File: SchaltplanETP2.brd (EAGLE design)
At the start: 110 x 60 mm, 59 parts, among them IC1 LM2674, IC2 ZXLD1350, IC3 ZXLD1350, IC4 ZXLD1350, IC5 ZXLD1350, M1 RN42_BLUETOOTH, T1 BUK98150-55A

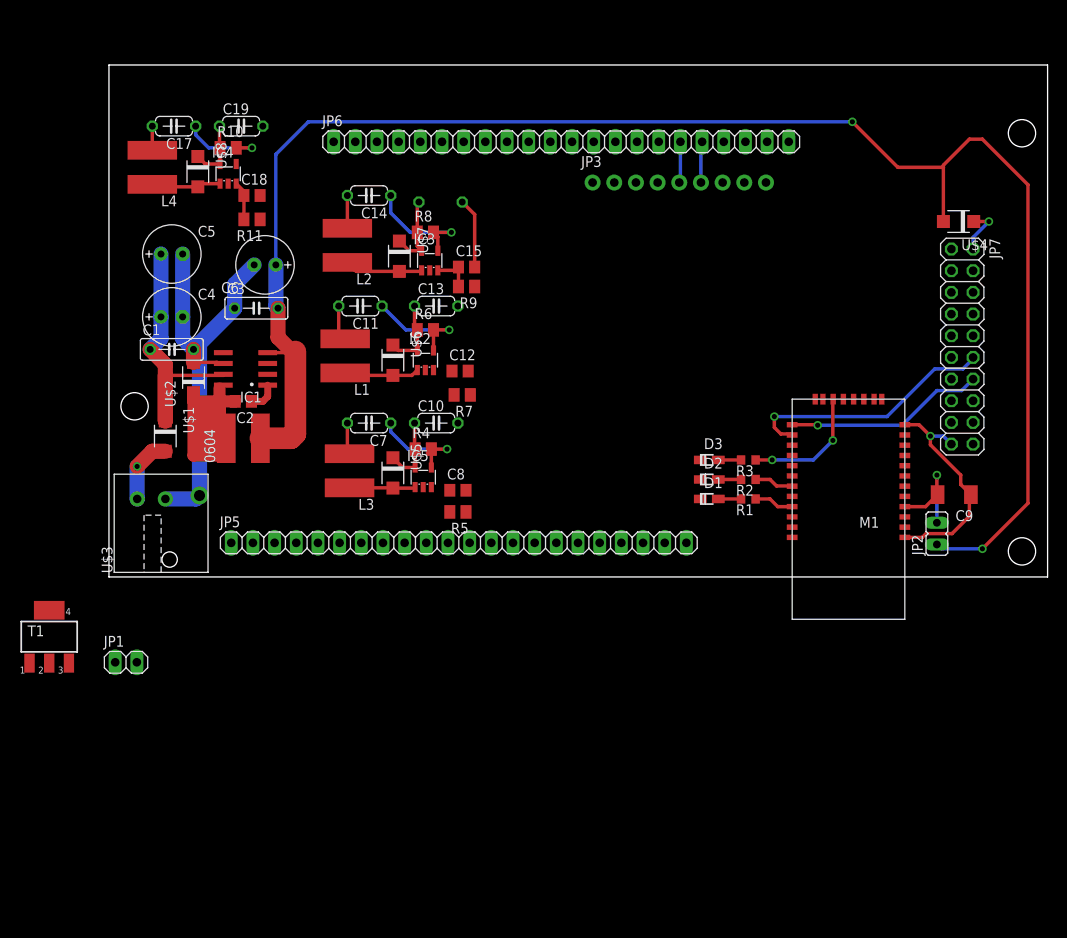
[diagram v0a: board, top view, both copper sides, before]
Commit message: Changed LED of pin 21 from the RN42 module to fit the datasheet. Added Jumpber behind DC-Jack to allow direct soldering of cables. Added Terminal Blocks for LEDs.
Placed part onto grid.
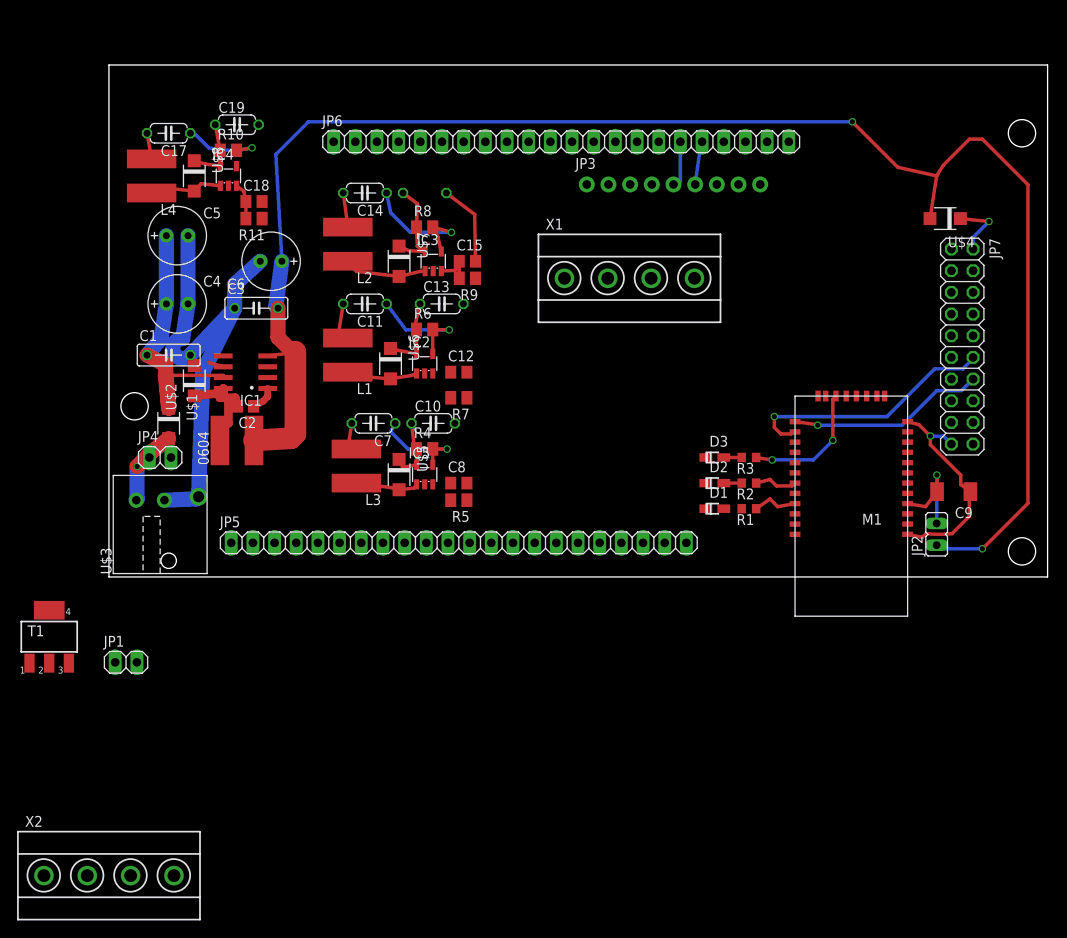
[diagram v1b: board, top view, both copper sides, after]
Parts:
- added JP4: (no value), pinhead:1X02
- added X1, X2: TERMINAL_BLOCK_MC000036, Moodlight:TERMINAL_BLOCK_MC000036
- R1: value 330 -> 220
- moved C5 2.25 mm to (8.00, 40.0)
- moved C16 2.14 mm to (37.0, 45.0)
- moved C4 1.65 mm to (8.00, 32.0)
- moved U$4 1.61 mm to (98.0, 42.0)
- moved U$1 1.54 mm to (7.00, 18.0)
- moved R5 1.38 mm to (41.0, 9.00)
- moved D1 1.31 mm to (71.0, 8.00)
- moved R1 1.15 mm to (75.0, 8.00)
- moved C17 1.04 mm to (7.00, 52.0)
- moved L4 1.01 mm to (5.00, 47.0)
- moved L3 0.98 mm to (29.0, 13.0)
- moved R9 0.97 mm to (42.0, 35.0)
- moved C8 0.85 mm to (41.0, 11.0)
- moved C6 0.83 mm to (19.0, 37.0)
- moved 0604 0.79 mm to (15.0, 16.0)
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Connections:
- removed net N$1: U$1.A, U$3.1
- new net +24V_EINGANG: JP4.1, U$1.A, U$3.1
- new net 4_LED+: X2.4
- new net 4_LED-: X2.3
- new net N$21: M1.22
- net +3V3: now also D1.A
- net 1_LED+: now also X1.2
- net 1_LED-: now also X1.1
- net 2_LED+: now also X1.4
- net 2_LED-: now also X1.3
- net 3_LED+: now also X2.2
- net 3_LED-: now also X2.1
- net GND: now also JP4.2; no longer D1.C
- net N$7: now also D1.C; no longer D1.A
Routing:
- net +24V_EINGANG: track 0.00 -> 8.93 mm, vias 0 -> 1
- net N$1: track 7.85 -> 0.00 mm, vias 1 -> 0
- net N$3: track 21.5 -> 14.1 mm
- net VCC: track 33.3 -> 36.3 mm
- net N$7: track 2.67 -> 0.00 mm
- net N$4: track 5.77 -> 7.36 mm
- net 2_LED+: track 14.6 -> 15.7 mm
- net GND: track 92.1 -> 93.1 mm
- net 0_LED-: track 3.69 -> 4.44 mm
- net N$18: track 8.21 -> 8.92 mm
- net IMP_TX: track 4.83 -> 5.53 mm
- net N$10: track 4.66 -> 5.32 mm
- net N$9: track 2.67 -> 2.10 mm
- net N$8: track 2.67 -> 2.10 mm
- net N$16: track 9.19 -> 9.71 mm

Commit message: added terminal header and connection
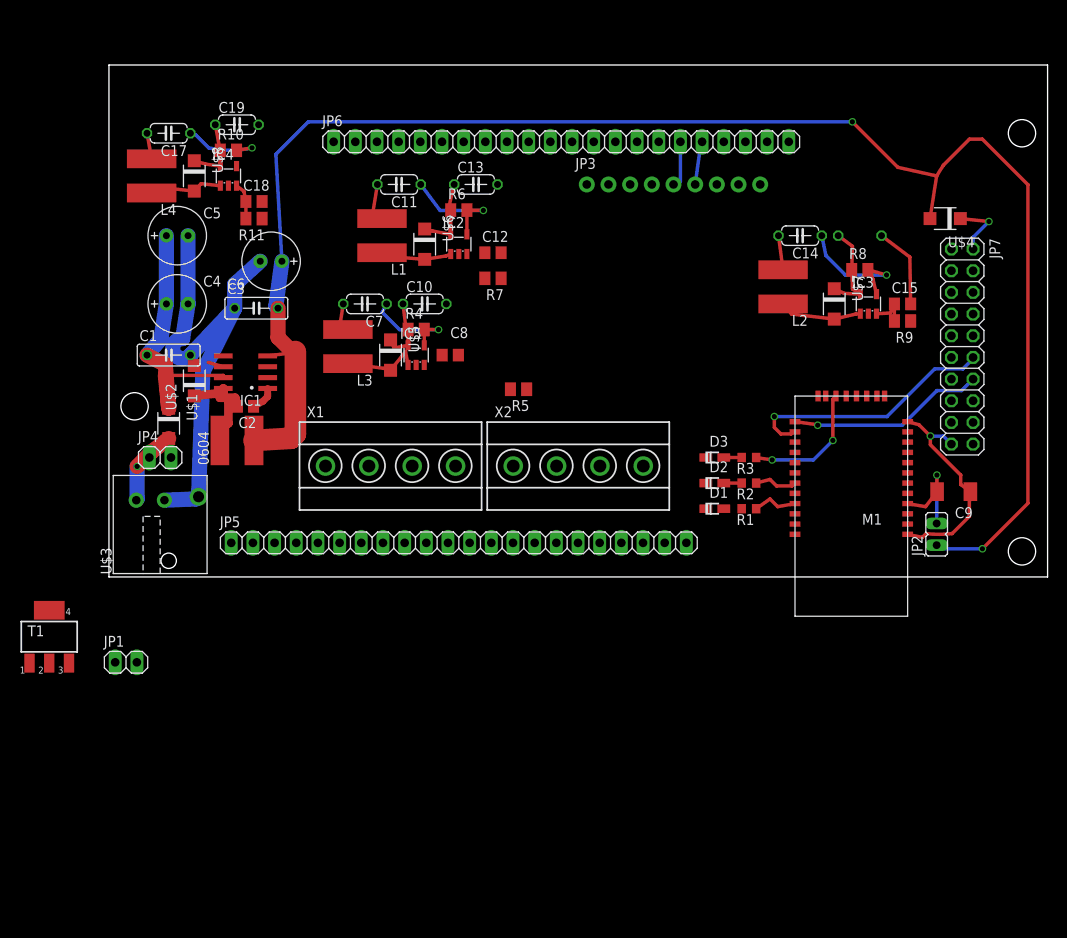
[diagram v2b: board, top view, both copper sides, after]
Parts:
- moved X2 73.0 mm to (55.0, 13.0)
- moved C14 51.2 mm to (81.0, 40.0)
- moved C15 51.2 mm to (93.0, 32.0)
- moved C16 51.2 mm to (88.0, 40.0)
- moved IC3 51.2 mm to (89.0, 32.0)
- moved L2 51.2 mm to (79.0, 34.0)
- moved R8 51.2 mm to (88.0, 36.0)
- moved R9 51.2 mm to (93.0, 30.0)
- moved U$7 51.2 mm to (85.0, 32.0)
- moved X1 35.6 mm to (33.0, 13.0)
- moved C8 15.0 mm to (40.0, 26.0)
- moved R5 14.8 mm to (48.0, 22.0)
- moved C11 14.6 mm to (34.0, 46.0)
- moved C12 14.6 mm to (45.0, 38.0)
- moved C13 14.6 mm to (43.0, 46.0)
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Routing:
- net N$6: track 7.36 -> 9.47 mm

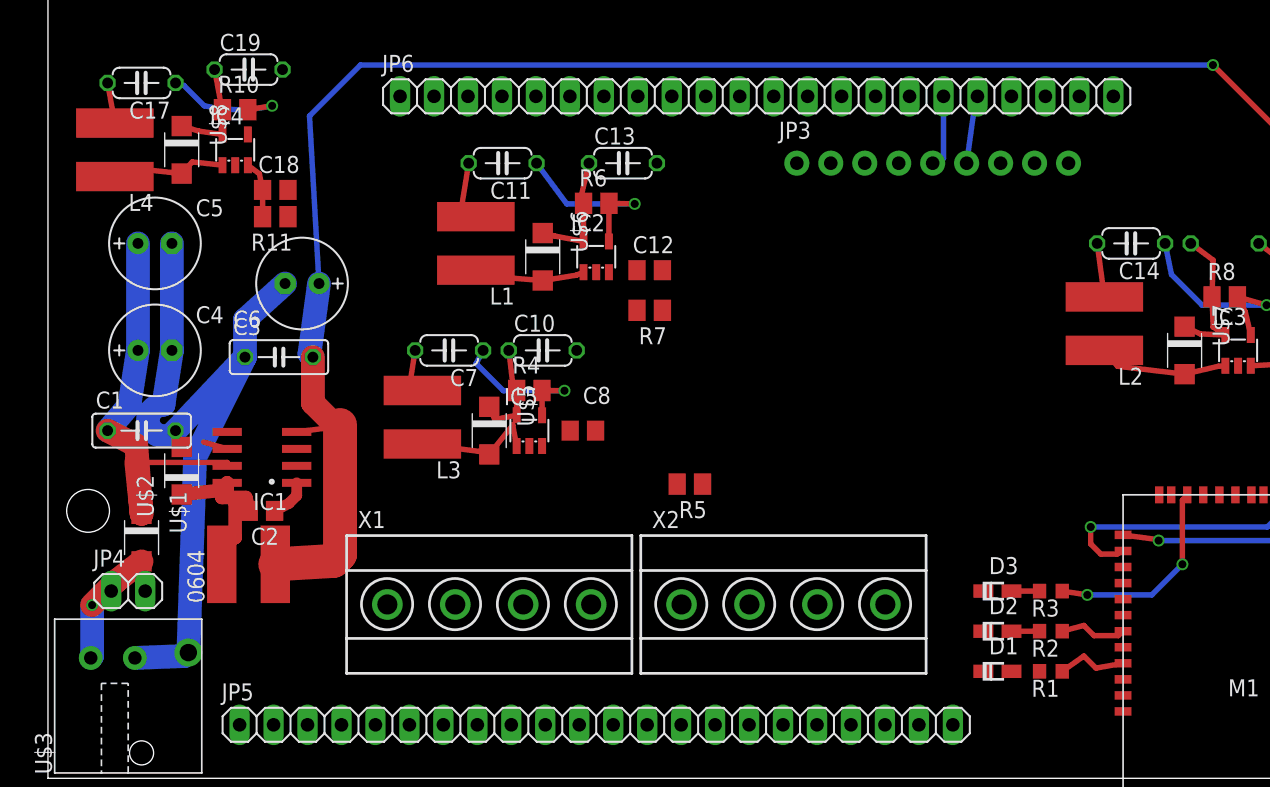
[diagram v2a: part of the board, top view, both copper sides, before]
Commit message: rearranged driver 1 and 2
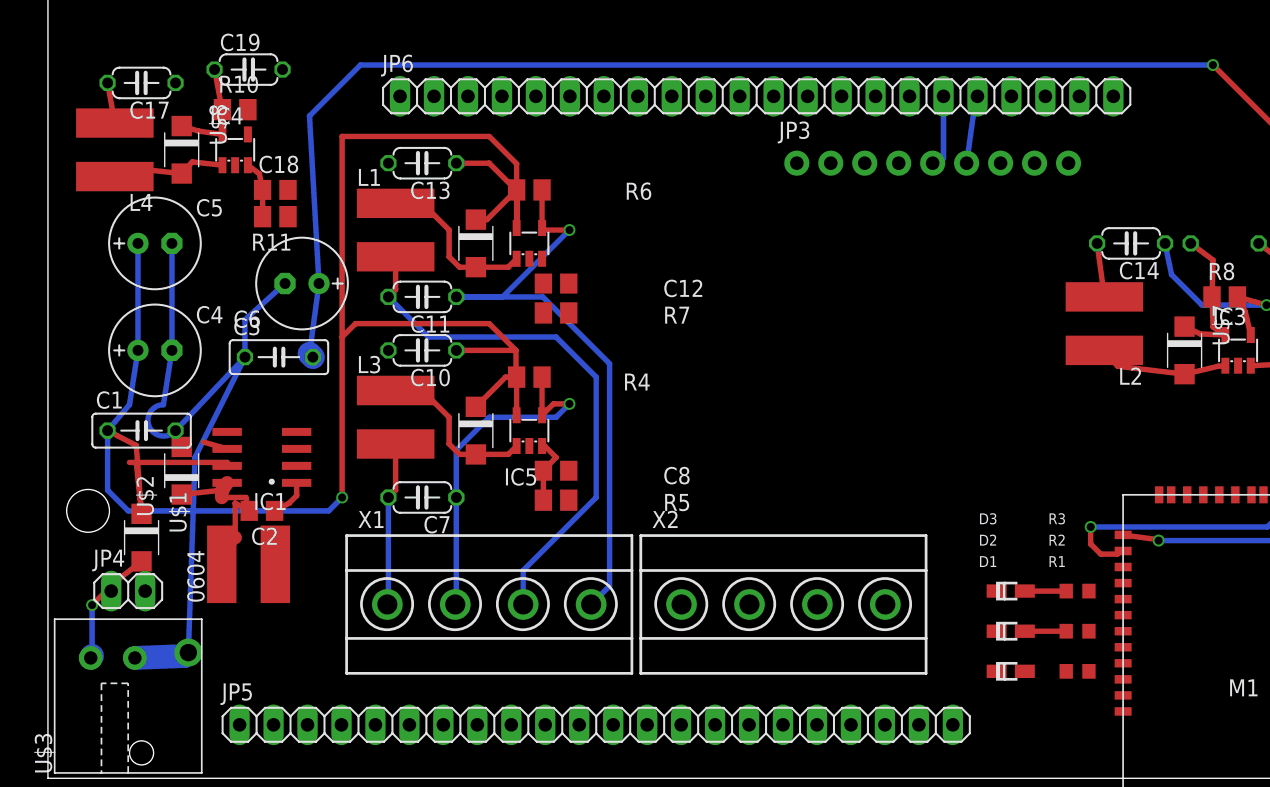
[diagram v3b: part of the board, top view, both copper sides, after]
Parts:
- D1: value GREEN -> G
- D2: value BLUE -> B
- D3: value YELLOW -> Y
- moved C13 15.0 mm to (28.0, 46.0), turned to 180 degrees
- moved C11 11.7 mm to (28.0, 36.0)
- moved C7 11.2 mm to (28.0, 21.0)
- moved R5 10.1 mm to (38.0, 20.8)
- moved C10 9.00 mm to (28.0, 32.0), turned to 180 degrees
- moved C12 7.07 mm to (38.0, 37.0)
- moved R7 7.00 mm to (38.0, 34.8)
- moved L1 6.08 mm to (26.0, 41.0), turned to 0 degrees
- moved IC2 5.10 mm to (36.0, 40.0)
- moved R6 5.10 mm to (36.0, 44.0)
- moved U$6 5.10 mm to (32.0, 40.0)
- moved C8 3.61 mm to (38.0, 23.0)
- moved L3 2.00 mm to (26.0, 27.0), turned to 0 degrees
- moved R1 2.00 mm to (77.0, 8.00)
- moved R2 2.00 mm to (77.0, 11.0)
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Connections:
- removed net 4_LED+: X2.4
- removed net 4_LED-: X2.3
- removed net VCC: C10.1, C13.1, C16.1, C19.1, IC2.5, IC3.5, IC4.5, IC5.5, R10.1, R4.1, R6.1, R8.1, U$5.C, U$6.C, U$7.C, U$8.C
- net +24V: now also C10.1, C13.1, C16.1, C19.1, IC2.5, IC3.5, IC4.5, IC5.5, R10.1, R4.1, R6.1, R8.1, U$5.C, U$6.C, U$7.C, U$8.C
- net 0_LED+: now also X1.2
- net 0_LED-: now also X1.1
- net 1_LED+: now also X1.4; no longer X1.2
- net 1_LED-: now also X1.3; no longer X1.1
- net 2_LED+: now also X2.2; no longer X1.4
- net 2_LED-: now also X2.1; no longer X1.3
- net 3_LED+: now also X2.4; no longer X2.2
- net 3_LED-: now also X2.3; no longer X2.1
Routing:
- net +24V: track 33.6 -> 164.3 mm, vias 0 -> 1
- net VCC: track 36.3 -> 0.00 mm
- net 1_LED-: track 4.64 -> 40.5 mm
- net 1_LED+: track 13.6 -> 47.6 mm
- net +3V3: track 193.8 -> 169.9 mm
- net N$12: track 15.3 -> 0.00 mm, vias 2 -> 0
- net 0_LED+: track 12.1 -> 26.7 mm, vias 1 -> 2
- net 3_LED+: track 9.72 -> 0.00 mm, vias 1 -> 0
- net 0_LED-: track 4.44 -> 12.3 mm, vias 0 -> 1
- net N$10: track 5.32 -> 0.00 mm
- net N$11: track 5.05 -> 0.00 mm
- net N$13: track 0.00 -> 4.98 mm
- net N$14: track 8.55 -> 12.5 mm
- net N$6: track 9.47 -> 12.5 mm
- net N$9: track 2.10 -> 3.10 mm
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
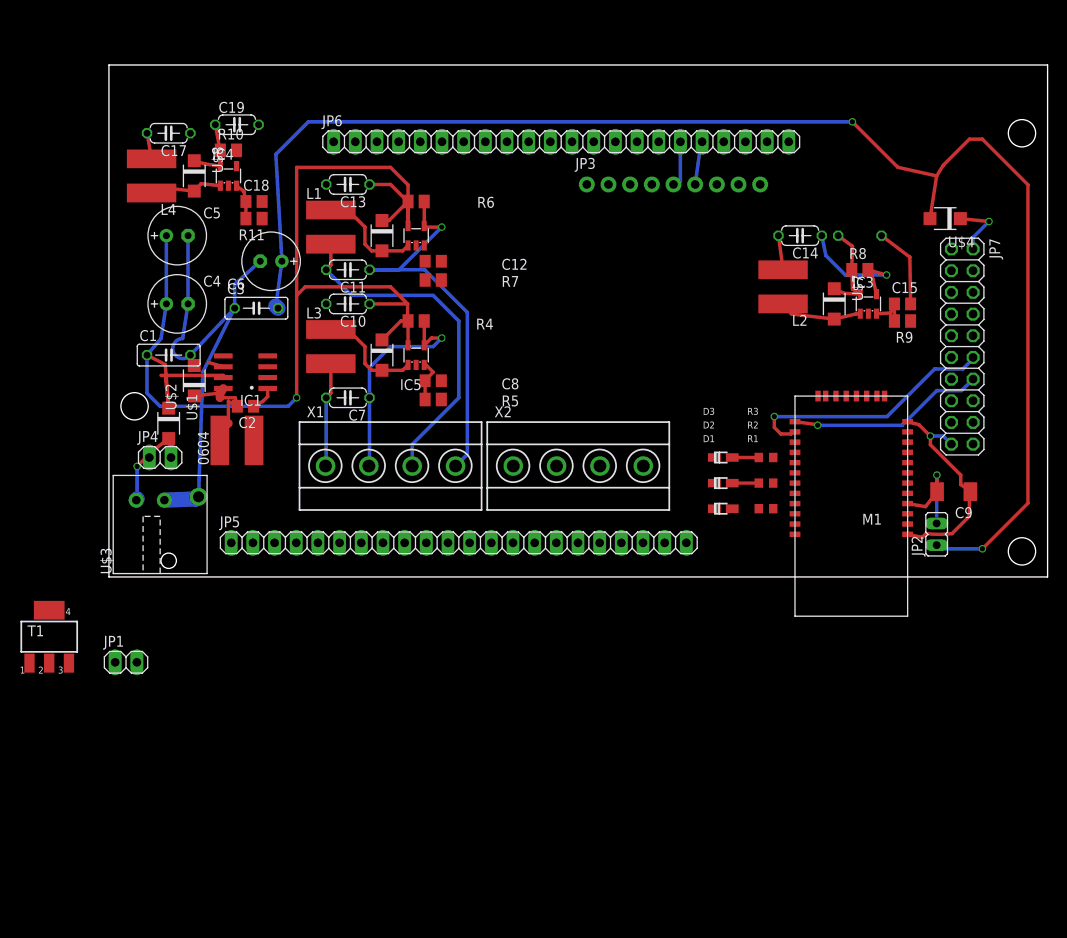
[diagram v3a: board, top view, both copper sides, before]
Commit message: placed driver 3 and 4
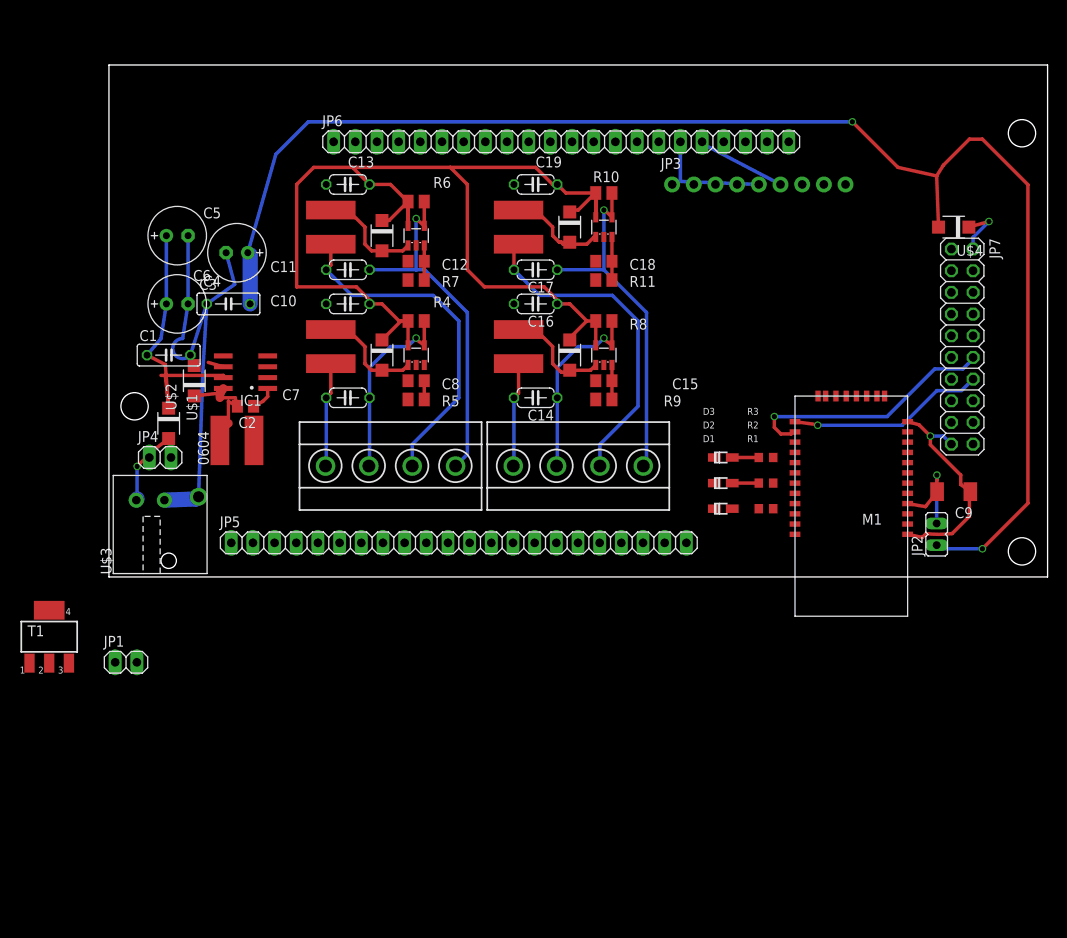
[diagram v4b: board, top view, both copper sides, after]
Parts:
- moved C17 45.9 mm to (50.0, 36.0)
- moved IC4 44.4 mm to (58.0, 41.0)
- moved U$8 44.4 mm to (54.0, 41.0)
- moved R10 44.3 mm to (58.0, 45.0)
- moved L4 43.4 mm to (48.0, 41.0), turned to 0 degrees
- moved R11 41.6 mm to (58.0, 34.8), turned to 0 degrees
- moved C18 41.6 mm to (58.0, 37.0), turned to 180 degrees
- moved C16 38.8 mm to (50.0, 32.0), flipped to the top
- moved C14 36.4 mm to (50.0, 21.0)
- moved R9 36.2 mm to (58.0, 20.8), turned to 0 degrees
- moved C15 36.1 mm to (58.0, 23.0), turned to 180 degrees
- moved C19 35.7 mm to (50.0, 46.0), turned to 180 degrees
- moved L2 31.8 mm to (48.0, 27.0), turned to 0 degrees
- moved IC3 31.6 mm to (58.0, 26.0)
- moved U$7 31.6 mm to (54.0, 26.0)
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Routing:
- net 3_LED+: track 0.00 -> 41.8 mm, vias 0 -> 1
- net 3_LED-: track 3.05 -> 39.1 mm
- net GND: track 93.1 -> 82.8 mm
- net IMP_TX: track 5.53 -> 13.8 mm
- net 2_LED-: track 4.04 -> 12.3 mm
- net 2_LED+: track 15.7 -> 22.9 mm
- net IMP_RX: track 5.10 -> 10.7 mm
- net 1_LED+: track 47.6 -> 42.7 mm
- net N$15: track 0.00 -> 4.05 mm
- net 0_LED+: track 26.7 -> 22.9 mm
- net N$18: track 8.92 -> 12.6 mm
- net +24V: track 164.3 -> 167.9 mm, vias 1 -> 0
- net N$16: track 9.71 -> 12.6 mm
- net N$13: track 4.98 -> 2.20 mm
- net N$4: track 7.36 -> 6.43 mm
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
